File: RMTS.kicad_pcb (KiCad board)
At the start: 2 copper layers, 80 x 50.2 mm, 55 parts, among them J1 USB_B, J10 CONN_02, J2 Programmer, J3 Screw_Terminal_01x03, J4 Screw_Terminal_01x04, J5 Screw_Terminal_01x02, J6 Screw_Terminal_01x02, J7 Micro_SD_Card_Det_Hirose_DM3AT, J8 CONN_03, J9 CONN_02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

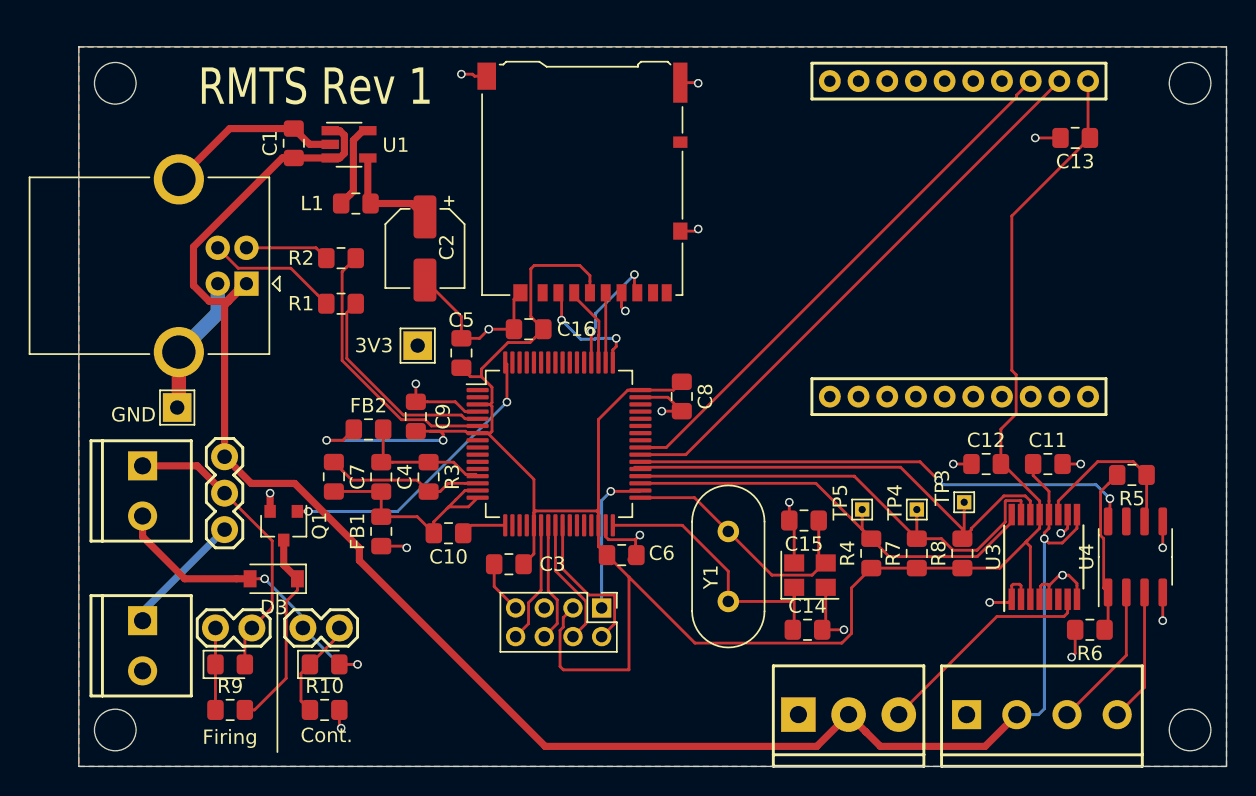
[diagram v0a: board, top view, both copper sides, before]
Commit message: Removed backup crystal, resized board
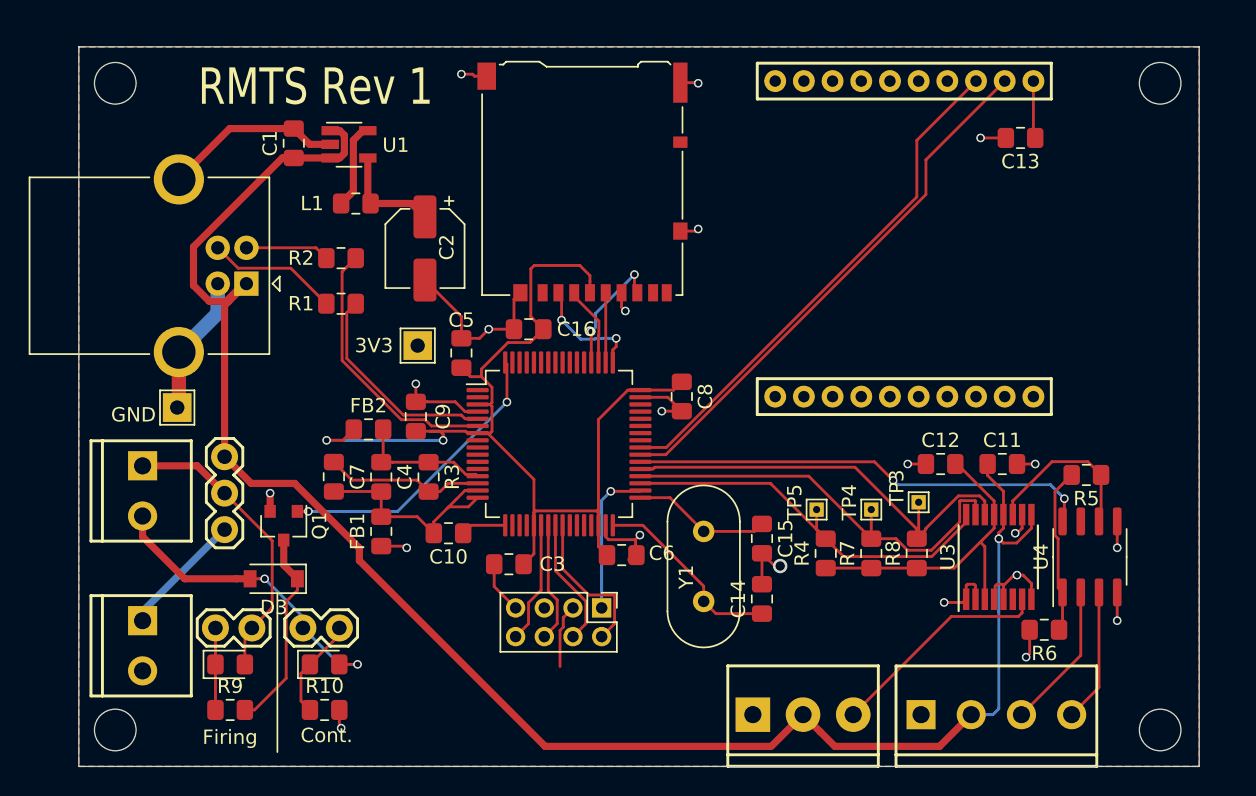
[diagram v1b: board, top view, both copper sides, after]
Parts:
- removed Y2: Crystal_GND24_Small, Crystal:Crystal_SMD_3225-4Pin_3.2x2.5mm
- moved C14 3.83 mm to (179.7, 100.7), turned to 90 degrees
- moved C13 3.81 mm to (197.7, 68.6)
- moved JP1 3.81 mm to (178.6, 75.6)
- moved C15 3.19 mm to (179.7, 96.5), turned to 270 degrees
- moved C12 3.18 mm to (192.2, 91.3)
- moved J3 3.18 mm to (179.1, 108.8)
- moved J4 3.18 mm to (190.8, 108.8)
- moved R5 3.18 mm to (202.3, 92.1)
- moved R6 3.18 mm to (199.4, 102.9)
- moved R7 3.18 mm to (187.3, 97.5)
- moved R8 3.18 mm to (190.5, 97.5)
- moved TP4 3.18 mm to (187.3, 94.5)
- moved TP5 3.18 mm to (183.5, 94.5)
- moved U4 3.18 mm to (202.6, 97.8)
- moved C11 3.17 mm to (196.5, 91.3)
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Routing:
- net +3V3: track 173.6 -> 111.7 mm
- net /XTAL2: track 18.7 -> 9.67 mm
- net /XTAL1: track 19.9 -> 13.6 mm
- net GND: track 94.3 -> 89.2 mm, vias 22 -> 21
- net /ADRDY: track 35.0 -> 31.5 mm
- net /VBUS: track 126.5 -> 123.2 mm
- net /ASDA: track 33.9 -> 30.8 mm
- net /ASCL: track 32.4 -> 29.2 mm
- net /AMP_EN: track 35.4 -> 32.3 mm
- net /DIN: track 40.0 -> 37.6 mm
- net /DOUT: track 37.9 -> 36.3 mm
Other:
- board size 80 x 50.2 mm -> 78.1 x 50.2 mm

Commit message: Added continuity optocoupler, capacitor pads to loadcell connection
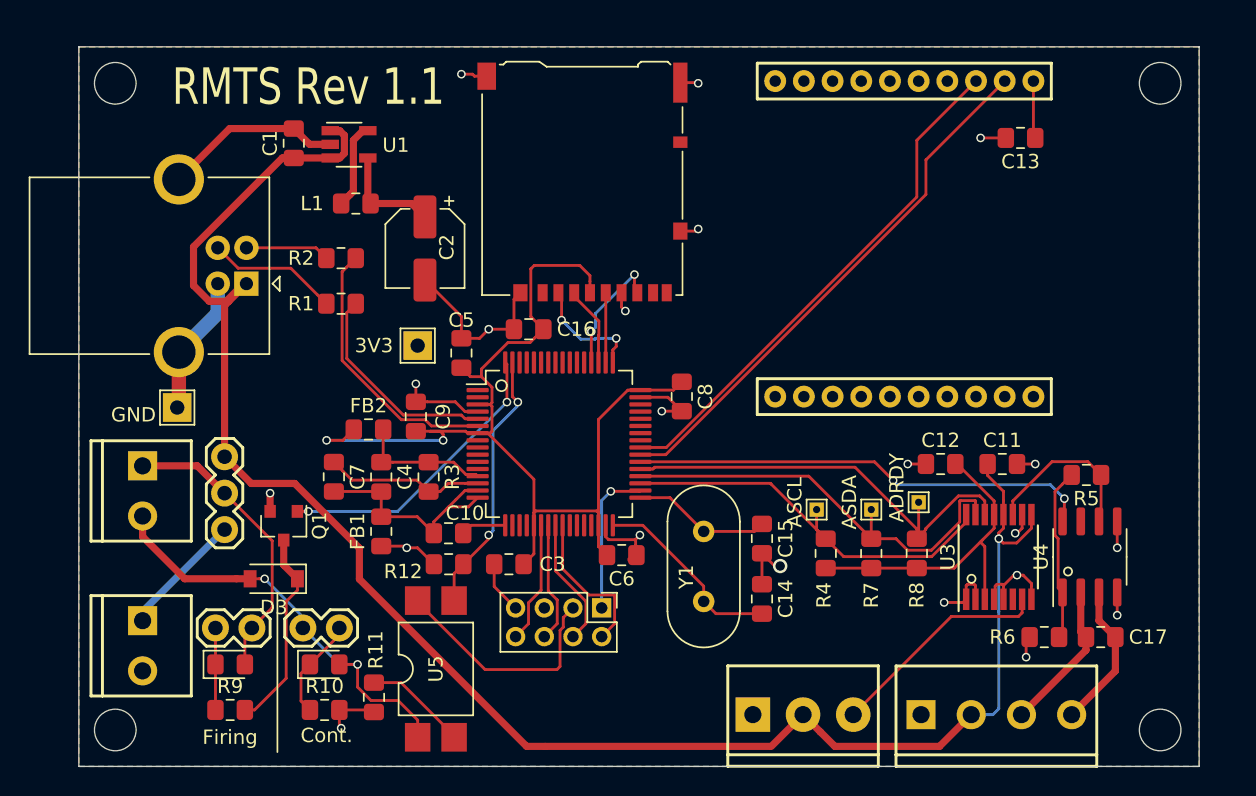
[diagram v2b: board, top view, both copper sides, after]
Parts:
- added C17: 0.47uF, Capacitor_SMD:C_0805_2012Metric_Pad1.15x1.40mm_HandSolder, F.Cu at (203.3, 103.4)
- added R11: 500, Resistor_SMD:R_0805_2012Metric_Pad1.15x1.40mm_HandSolder, F.Cu at (152.7, 107.6)
- added R12: 500, Resistor_SMD:R_0805_2012Metric_Pad1.15x1.40mm_HandSolder, F.Cu at (157.9, 98.3)
- added U5: LTV-817S, Package_DIP:SMDIP-4_W9.53mm, F.Cu at (157.0, 105.6)
- moved R6 0.51 mm to (199.4, 103.4)
- renumbered TP3 to ADRDY, TP5 to ASCL, TP4 to ASDA
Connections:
- U2 pad 63: Net-(U2-Pad63) -> /CONT
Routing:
- net /CONT: track 0.00 -> 18.6 mm, vias 0 -> 2
- net +3V3: track 111.7 -> 123.8 mm
- net Net-(D2-Pad2): track 22.0 -> 29.9 mm
- net Net-(R11-Pad1): track 0.00 -> 7.23 mm
- net GND: track 89.2 -> 93.1 mm
- net Net-(C17-Pad1): track 9.31 -> 10.3 mm
- net /VBUS: track 123.2 -> 124.0 mm
- net /FG0: track 11.6 -> 12.1 mm
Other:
- board text added: "RMTS Rev 1.1"
- board text removed: "RMTS Rev 1"

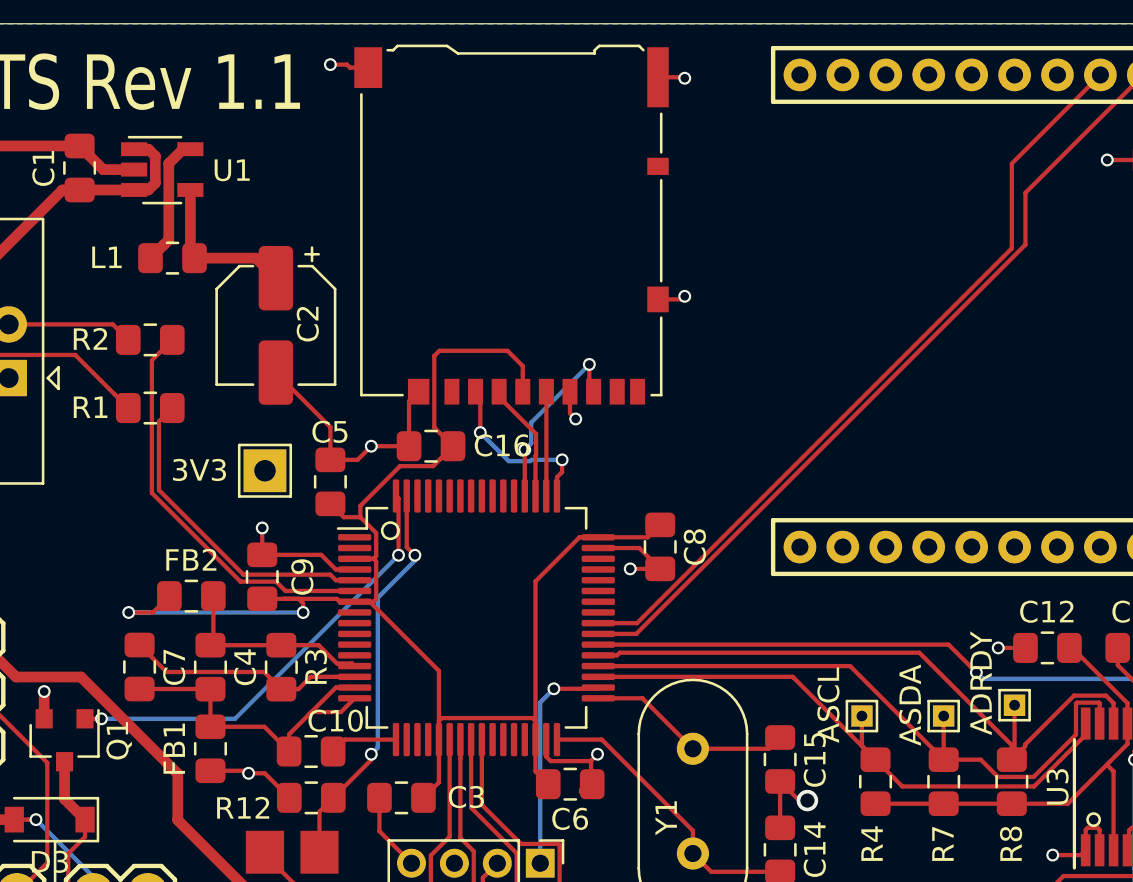
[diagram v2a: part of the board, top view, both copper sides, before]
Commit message: Added resistor to avoid battery shutting off
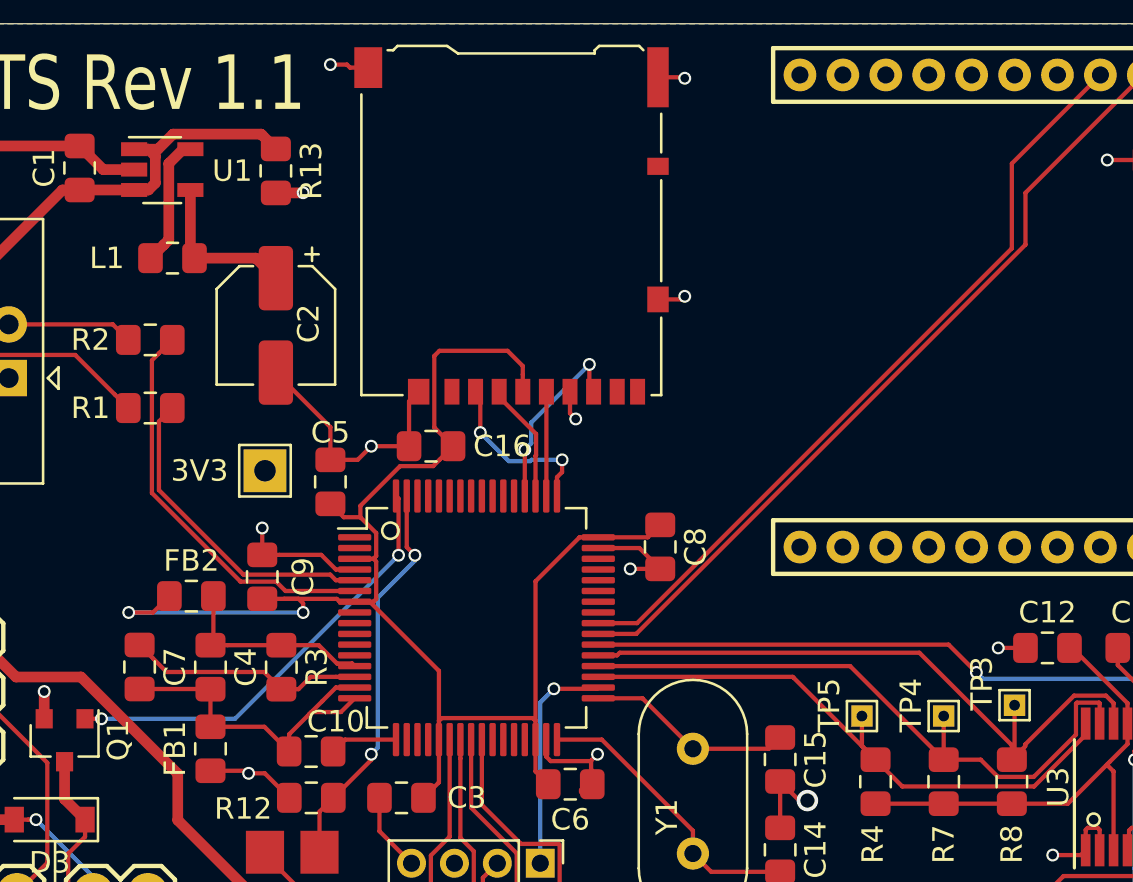
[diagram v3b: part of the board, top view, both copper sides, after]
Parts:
- added R13: 500, Resistor_SMD:R_0805_2012Metric_Pad1.15x1.40mm_HandSolder, F.Cu at (156.2, 69.1)
- renumbered ADRDY to TP3, ASDA to TP4, ASCL to TP5
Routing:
- net /VBUS: track 124.0 -> 131.1 mm
- net GND: track 93.1 -> 94.4 mm, vias 21 -> 22
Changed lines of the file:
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@@
     (thickness 1.6)
     (drawings 25)
-    (tracks 500)
+    (tracks 508)
     (zones 0)
-    (modules 58)
+    (modules 59)
     (nets 95)
   )
@@
   )
   (setup
-    (last_trace_width 0.2)
+    (last_trace_width 0.5)
     (user_trace_width 0.5)
     (user_trace_width 1)
@@
     (uvia_drill 0.1)
   )
+  (module Resistor_SMD:R_0805_2012Metric_Pad1.15x1.40mm_HandSolder (layer F.Cu)
+    (at 156.21 69.088 270)
+    (descr "Resistor SMD 0805 (2012 Metric), square (rectangular) end terminal, IPC_7351 nominal with elongated pad for handsoldering. (Body size source: https://docs.google.com/spreadsheets/d/1BsfQQcO9C6DZCsRaXUlFlo91Tg2WpOkGARC1WS5S8t0/edit?usp=sharing), generated with kicad-footprint-generator")
+    (tags "resistor handsolder")
+    (attr smd)
+    (fp_text reference R13 (at 0 -1.65 90) (layer F.SilkS)
+      (effects (font (size 1 1) (thickness 0.15)))
+    )
+    (fp_text value 500 (at 0 1.65 90) (layer F.Fab)
+      (effects (font (size 1 1) (thickness 0.15)))
+    )
+    (fp_text user %R (at 0 0 90) (layer F.Fab)
+      (effects (font (size 0.5 0.5) (thickness 0.08)))
+    )
+    (fp_line (start 1.85 0.95) (end -1.85 0.95) (layer F.CrtYd) (width 0.05))
+    (fp_line (start 1.85 -0.95) (end 1.85 0.95) (layer F.CrtYd) (width 0.05))
+    (fp_line (start -1.85 -0.95) (end 1.85 -0.95) (layer F.CrtYd) (width 0.05))
+    (fp_line (start -1.85 0.95) (end -1.85 -0.95) (layer F.CrtYd) (width 0.05))
+    (fp_line (start -0.261252 0.71) (end 0.261252 0.71) (layer F.SilkS) (width 0.12))
+    (fp_line (start -0.261252 -0.71) (end 0.261252 -0.71) (layer F.SilkS) (width 0.12))
+    (fp_line (start 1 0.6) (end -1 0.6) (layer F.Fab) (width 0.1))
+    (fp_line (start 1 -0.6) (end 1 0.6) (layer F.Fab) (width 0.1))
+    (fp_line (start -1 -0.6) (end 1 -0.6) (layer F.Fab) (width 0.1))
+    (fp_line (start -1 0.6) (end -1 -0.6) (layer F.Fab) (width 0.1))
+    (pad 2 smd roundrect (at 1.025 0 270) (size 1.15 1.4) (layers F.Cu F.Paste F.Mask) (roundrect_rratio 0.217391)
+      (net 1 GND))
+    (pad 1 smd roundrect (at -1.025 0 270) (size 1.15 1.4) (layers F.Cu F.Paste F.Mask) (roundrect_rratio 0.217391)
+      (net 2 /VBUS))
+    (model ${KISYS3DMOD}/Resistor_SMD.3dshapes/R_0805_2012Metric.wrl
+      (at (xyz 0 0 0))
+      (scale (xyz 1 1 1))
+      (rotate (xyz 0 0 0))
+    )
+  )
   (module Package_DIP:SMDIP-4_W9.53mm (layer F.Cu)
     (at 156.972 105.598 90)
@@
     (tags "test point THT pad rectangle square")
     (attr virtual)
-    (fp_text reference ASCL (at -1.524 -0.508 90) (layer F.SilkS)
+    (fp_text reference TP5 (at -1.524 -0.508 90) (layer F.SilkS)
       (effects (font (size 1 1) (thickness 0.15)))
     )
@@
     (tags "test point THT pad rectangle square")
     (attr virtual)
-    (fp_text reference ASDA (at -1.524 -0.508 90) (layer F.SilkS)
+    (fp_text reference TP4 (at -1.524 -0.508 90) (layer F.SilkS)
       (effects (font (size 1 1) (thickness 0.15)))
     )
@@
     (tags "test point THT pad rectangle square")
     (attr virtual)
-    (fp_text reference ADRDY (at -1.524 -1.016 90) (layer F.SilkS)
+    (fp_text reference TP3 (at -1.524 -1.016 90) (layer F.SilkS)
       (effects (font (size 1 1) (thickness 0.15)))
     )
@@
   (segment (start 155.693 97.155) (end 154.94 97.155) (width 0.2) (layer F.Cu) (net 1))
   (segment (start 156.836 98.298) (end 155.693 97.155) (width 0.2) (layer F.Cu) (net 1))
+  (via (at 157.48 70.104) (size 0.6) (drill 0.4) (layers F.Cu B.Cu) (net 1))
+  (segment (start 157.471 70.113) (end 157.48 70.104) (width 0.5) (layer F.Cu) (net 1))
+  (segment (start 156.21 70.113) (end 157.471 70.113) (width 0.5) (layer F.Cu) (net 1))
   (segment (start 146.831 70.212) (end 147.066 69.977) (width 0.2) (layer F.Cu) (net 2))
   (via (at 196.215 96.52) (size 0.6) (drill 0.4) (layers F.Cu B.Cu) (net 2))
@@
   (segment (start 151.638 99.337602) (end 163.298398 110.998) (width 0.5) (layer F.Cu) (net 2))
   (segment (start 163.298398 110.998) (end 164.592 110.998) (width 0.5) (layer F.Cu) (net 2))
+  (segment (start 155.586628 67.439628) (end 156.21 68.063) (width 0.5) (layer F.Cu) (net 2))
+  (segment (start 155.521999 67.374999) (end 155.586628 67.439628) (width 0.5) (layer F.Cu) (net 2))
+  (segment (start 151.418001 67.374999) (end 155.521999 67.374999) (width 0.5) (layer F.Cu) (net 2))
+  (segment (start 150.716 68.077) (end 151.418001 67.374999) (width 0.5) (layer F.Cu) (net 2))
+  (segment (start 149.606 68.077) (end 150.716 68.077) (width 0.5) (layer F.Cu) (net 2))
   (segment (start 173.536999 86.160001) (end 174.117 85.58) (width 0.2) (layer F.Cu) (net 3))
   (segment (start 171.232001 86.160001) (end 173.536999 86.160001) (width 0.2) (layer F.Cu) (net 3))

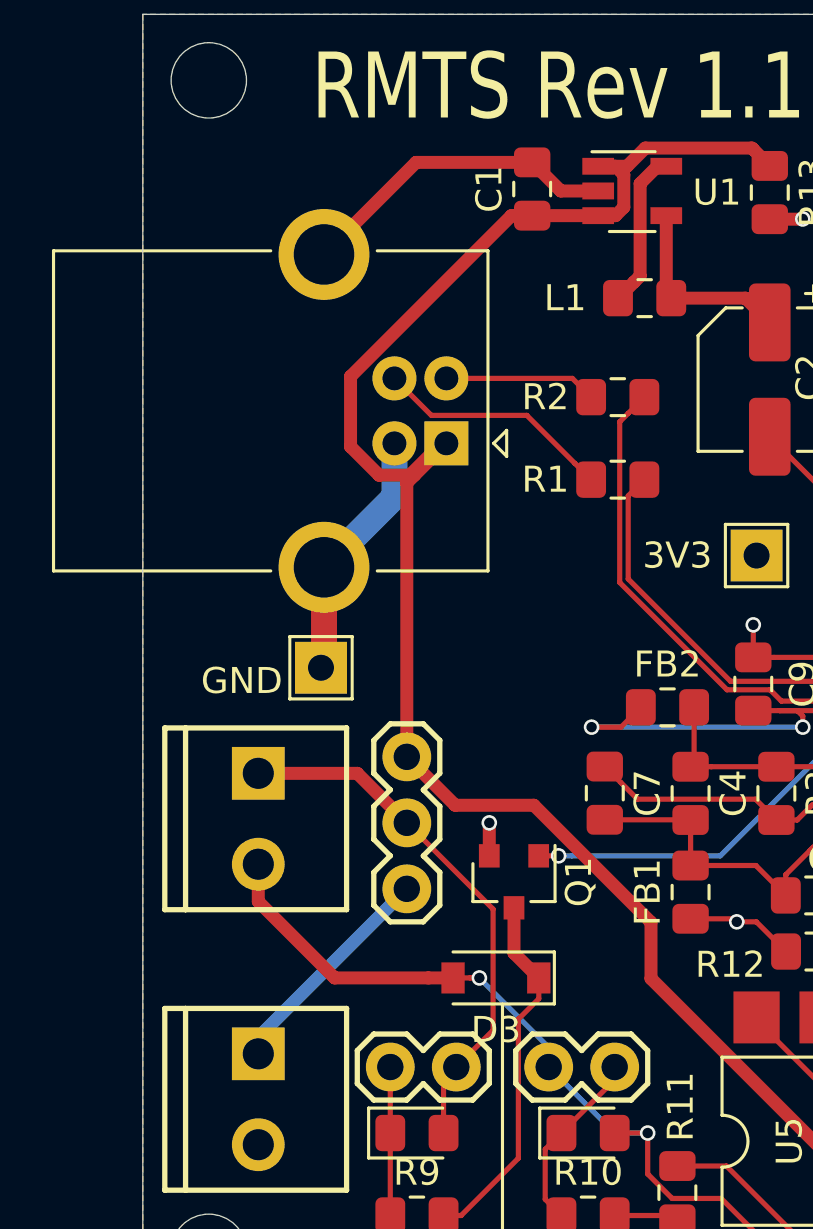
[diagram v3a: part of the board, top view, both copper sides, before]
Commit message: Removed USB pyro power jumper
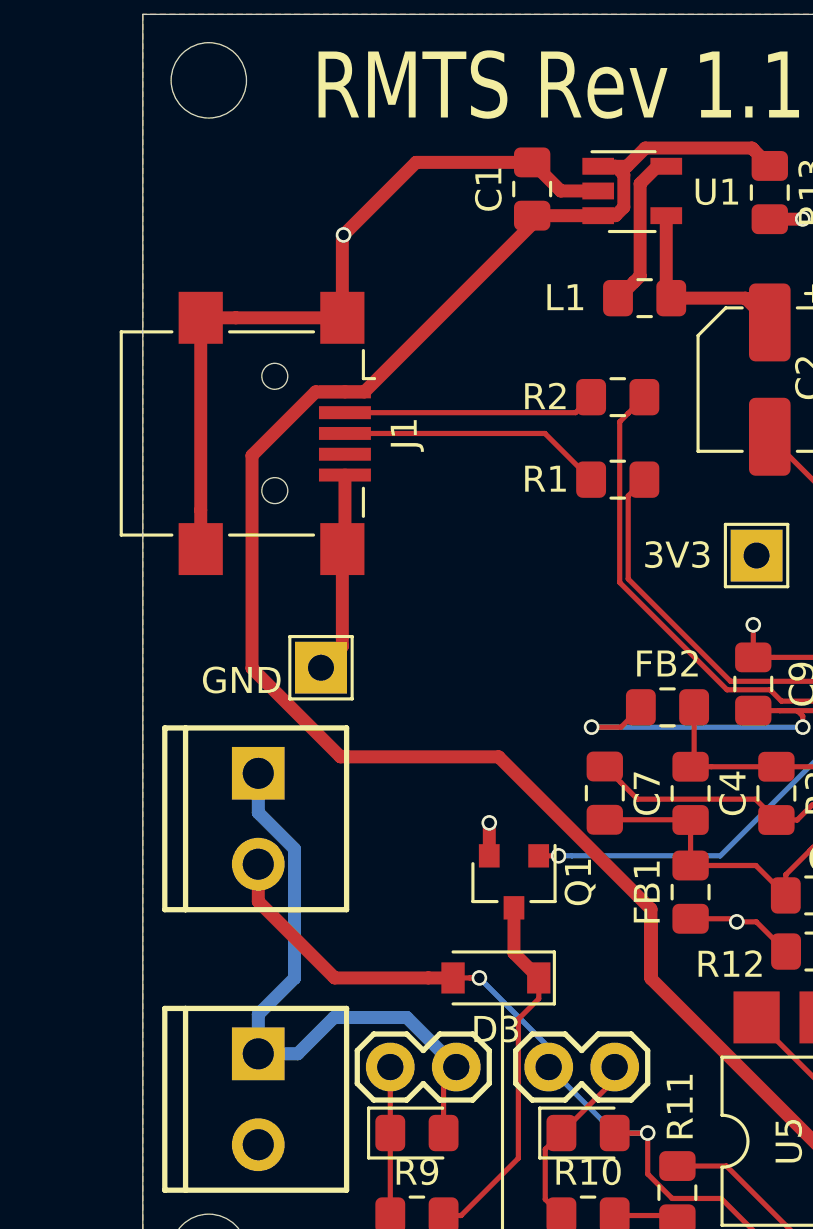
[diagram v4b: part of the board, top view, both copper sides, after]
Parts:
- removed J8: CONN_03, Connectors:1X03
- J1: value USB_B -> USB_B_Mini; footprint Connector_USB:USB_B_OST_USB-B1HSxx_Horizontal -> Connector_USB:USB_Mini-B_Lumberg_2486_01_Horizontal
- moved J1 6.61 mm to (137.2, 78.4), turned to 270 degrees
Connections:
- J1 pad 4: GND -> Net-(J1-Pad4)
- J5 pad 1: Net-(J5-Pad1) -> Net-(D1-Pad2)
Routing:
- net GND: track 94.4 -> 109.1 mm, vias 22 -> 23
- net Net-(J5-Pad1): track 9.93 -> 0.00 mm
- net Net-(D1-Pad2): track 20.6 -> 24.9 mm
- net Net-(J1-Pad2): track 5.87 -> 9.72 mm
- net /VBUS: track 131.1 -> 134.4 mm
- net Net-(J1-Pad3): track 9.18 -> 10.2 mm
